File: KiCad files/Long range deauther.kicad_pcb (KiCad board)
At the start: 2 copper layers, 42 x 16 mm, 29 parts, among them J1 USB-AM-S-X-X-TH, Q1 BC847, Q2 BC847, SW1 SW_Flash, SW2 SW_RST, U1 NCP1117-3.3_SOT223, U2 CP2102N-A02-GQFN28, U3 ESP-WROOM-02U

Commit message: next update with some update on pcb
these updates are for use and for production.
Changes are quickly listed in the changes.txt
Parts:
- removed D1: SP0503BAHT, Package_TO_SOT_SMD:SOT-143
- removed the G*** at (164.1, 88.8)
- removed the REF** at (164.0, 78.2)
- removed the REF** at (164.0, 83.0)
- added C5: 10uF, Capacitor_SMD:C_0805_2012Metric_Pad1.15x1.40mm_HandSolder, B.Cu at (156.0, 76.4)
- added C6: 4.7uF, Capacitor_SMD:C_0805_2012Metric_Pad1.15x1.40mm_HandSolder, B.Cu at (134.2, 78.2)
- added C7: 10uF, Capacitor_SMD:C_0805_2012Metric_Pad1.15x1.40mm_HandSolder, B.Cu at (156.4, 78.3)
- added C8: 100nF, Capacitor_SMD:C_0805_2012Metric_Pad1.15x1.40mm_HandSolder, B.Cu at (156.4, 80.2)
- added FB1: Ferrite_Bead, Capacitor_SMD:C_0805_2012Metric_Pad1.15x1.40mm_HandSolder, B.Cu at (134.2, 87.8)
- added G***: LOGO, spacehunh:CHICKEN_3-9_4-2_logo, F.Cu at (135.4, 83.2)
- added REF**: SMA_Horizontal, Long_range_deauther:SMA_Horizontal, F.Cu at (164.0, 83.0)
- C1: value 4.7uF -> 10nF
- C2: value 0.1uF -> 47pF
- C3: value 4.7uF -> 47pF
- C4: value 0.1uF -> 100nF
- J1: value USB-AM-S-X-X-TH -> USB_A; footprint Deauth_usb:SAMTEC_USB-AM-S-X-X-TH -> Connector_USB:USB_A_CNCTech_1001-011-01101_Horizontal
- R1: value 22.1K -> 10K
- R10, R11: value 470 -> 10K
- R2: value 47.5K -> 27R
- R3: value 1K -> 27R
- R6, R7: value 10K -> 470
- SW1: value SW_Flash -> SW_RST; footprint Button_Switch_SMD:SW_Push_SPST_NO_Alps_SKRK -> Long_range_deauther:HYP_1TS003B-1600-3500A-CT
- SW2: value SW_RST -> SW_Flash; footprint Button_Switch_SMD:SW_Push_SPST_NO_Alps_SKRK -> Long_range_deauther:HYP_1TS003B-1600-3500A-CT
- U1: value NCP1117-3.3_SOT223 -> AP2112-3.3; footprint Package_TO_SOT_SMD:SOT-223-3_TabPin2 -> Long_range_deauther:AP2112_REGULATOR
- U2: value CP2102N-A02-GQFN28 -> FT231XS; footprint Deauth_usb:CP2102N-A02-GQFN28 -> Package_SO:SSOP-20_3.9x8.7mm_P0.635mm
- U3: footprint Deauth_usb:ESP-WROOM-02U -> Long_range_deauther:ESP-WROOM-02U
- moved U1 17.5 mm to (153.2, 76.6), turned to 270 degrees
- moved R3 13.8 mm to (134.2, 84.0)
- moved C3 12.5 mm to (134.2, 80.1), turned to 0 degrees
- moved R11 12.2 mm to (139.2, 82.9)
- moved R2 9.59 mm to (134.2, 82.0), turned to 180 degrees
- moved R1 9.47 mm to (139.2, 86.7)
- moved C4 9.34 mm to (137.9, 78.2), turned to 0 degrees
- moved Q2 7.69 mm to (152.6, 81.6), turned to 90 degrees
- moved J1 7.32 mm to (121.7, 83.0), turned to 180 degrees
- moved R12 4.81 mm to (156.5, 87.8)
- moved R6 4.81 mm to (156.5, 82.1)
- moved R8 4.81 mm to (156.5, 85.9)
- moved R9 4.81 mm to (156.5, 84.0)
- moved R7 4.81 mm to (156.5, 89.7)
- moved R10 4.74 mm to (139.2, 84.8), turned to 180 degrees
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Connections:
- C1 pad 1: +5V -> Net-(C1-Pad1)
- C2 pad 1: +5V -> GND
- C2 pad 2: GND -> /J_N
- C3 pad 1: +3V3 -> /J_P
- C4 pad 1: +3V3 -> +5V
- R10 pad 1: Net-(R10-Pad1) -> +3V3
- R10 pad 2: TXD -> E_IO0
- R11 pad 1: RXD -> +3V3
- R11 pad 2: Net-(R11-Pad2) -> E_RST
- R12 pad 1: +3V3 -> GND
- R12 pad 2: E_RST -> E_IO15
- R2 pad 1: Net-(R1-Pad2) -> D+
- R2 pad 2: GND -> /J_P
- R3 pad 1: +3V3 -> /J_N
- R3 pad 2: Net-(R3-Pad2) -> D-
- R6 pad 1: +3V3 -> RXD
- R6 pad 2: E_IO0 -> Net-(R6-Pad2)
- R7 pad 1: +3V3 -> Net-(R7-Pad1)
- R7 pad 2: E_EN -> TXD
- R8 pad 1: GND -> +3V3
- R8 pad 2: E_IO15 -> E_EN
- SW1 pad 1: E_IO0 -> E_RST
- SW2 pad 1: E_RST -> E_IO0
- U1 pad 1: GND -> +5V
- U1 pad 2: +3V3 -> GND
- U1 pad 3: +5V -> Net-(R1-Pad2)
- U2 pad 1: Net-(U2-Pad1) -> DTR
- U2 pad 10: (no net) -> Net-(U2-Pad10)
- U2 pad 11: Net-(U2-Pad11) -> D+
- U2 pad 12: Net-(U2-Pad12) -> D-
- U2 pad 13: Net-(U2-Pad13) -> FTDI_100nF_TG
- U2 pad 14: Net-(U2-Pad14) -> FTDI_100nF_TG
- U2 pad 15: Net-(U2-Pad15) -> +5V
- U2 pad 16: Net-(U2-Pad16) -> GND
- U2 pad 2: Net-(U2-Pad2) -> CP_RST
- U2 pad 20: Net-(U2-Pad20) -> TXD
- U2 pad 3: GND -> FTDI_100nF_TG
- U2 pad 4: D+ -> RXD
- U2 pad 5: D- -> Net-(U2-Pad5)
- U2 pad 6: +3V3 -> GND
- U2 pad 7: +3V3 -> Net-(U2-Pad7)
- U2 pad 8: Net-(R1-Pad2) -> Net-(U2-Pad8)
- U2 pad 9: Net-(R3-Pad2) -> Net-(U2-Pad9)
- U3 pad 11: Net-(R10-Pad1) -> Net-(R7-Pad1)
- U3 pad 12: Net-(R11-Pad2) -> Net-(R6-Pad2)
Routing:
- net Net-(R7-Pad1): track 0.00 -> 29.4 mm, vias 0 -> 3
- net Net-(R6-Pad2): track 0.00 -> 28.8 mm, vias 0 -> 1
- net FTDI_100nF_TG: track 0.00 -> 24.1 mm, vias 0 -> 2
- net TXD: track 7.77 -> 26.7 mm, vias 2 -> 6
- net E_IO15: track 0.88 -> 13.9 mm
- net +3V3: track 64.7 -> 52.4 mm, vias 4 -> 7
- net Net-(R11-Pad2): track 11.1 -> 0.00 mm, vias 3 -> 0
- net Net-(C1-Pad1): track 0.00 -> 10.9 mm, vias 0 -> 1
- net E_IO0: track 42.3 -> 32.3 mm, vias 1 -> 2
- net Net-(R1-Pad2): track 10.6 -> 20.3 mm
- net /J_N: track 0.00 -> 9.12 mm, vias 0 -> 1
- net /J_P: track 0.00 -> 9.08 mm, vias 0 -> 1
- net GND: track 42.2 -> 51.0 mm, vias 8 -> 10
- net D-: track 20.8 -> 12.2 mm
- net D+: track 21.1 -> 12.8 mm
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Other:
- board size 42 x 16 mm -> 43 x 16 mm
- board text added: "F"
- board text added: "JLCJLCJLCJLC"
- board text added: "R"

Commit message: Add artwork  on to pcb
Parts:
- added G***: LOGO, Art:back, B.Cu at (150.7, 82.8)
- added G***: LOGO, Art:front, F.Cu at (164.2, 83.3)

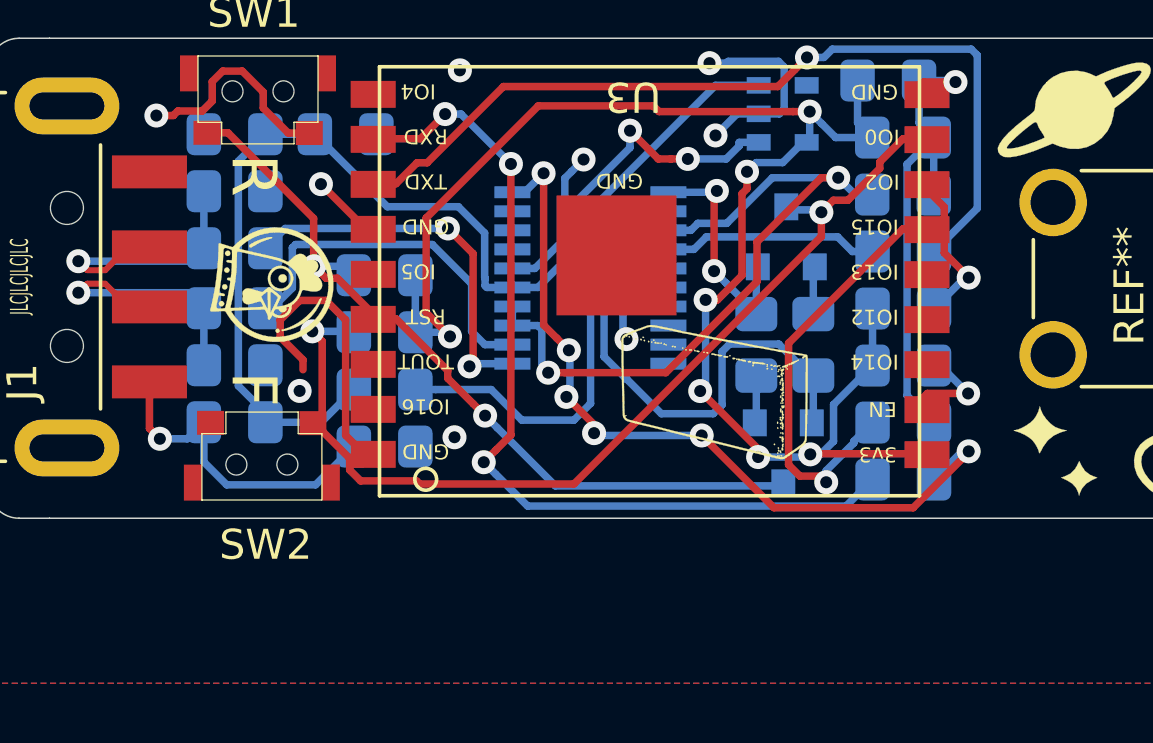
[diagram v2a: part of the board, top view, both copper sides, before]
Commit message: Will need to verify if these are right and if kicad has some issue with github or something. when opening the file after a day or after a git action some copper traces apear to change.
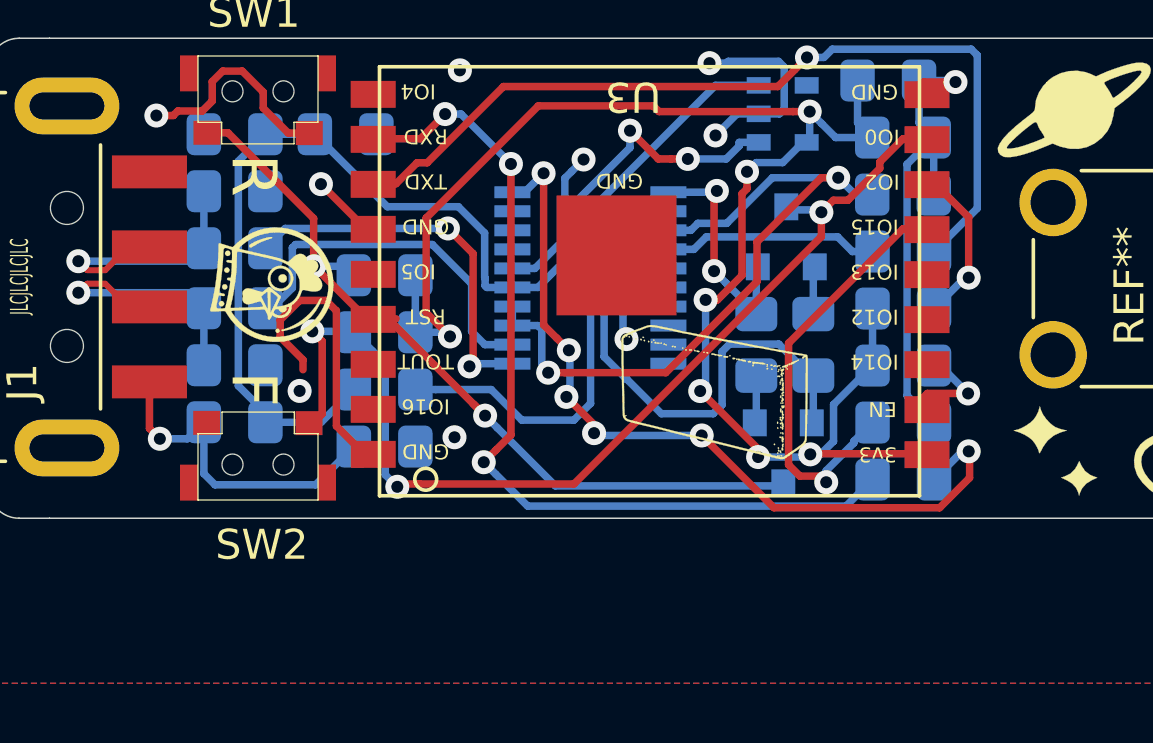
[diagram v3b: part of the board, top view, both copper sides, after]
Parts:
- moved SW2 0.13 mm to (134.9, 89.2)
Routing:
- net E_IO0: track 32.3 -> 34.3 mm, vias 2 -> 3
- net E_RST: track 26.6 -> 27.6 mm
- net TXD: track 26.7 -> 27.2 mm

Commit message: inbetween push to pull on linux
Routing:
- net FTDI_100nF_TG: track 24.1 -> 25.1 mm
- net GND: track 51.0 -> 50.2 mm
- net Net-(R1-Pad2): track 20.3 -> 19.5 mm
- net +5V: track 37.4 -> 36.8 mm
